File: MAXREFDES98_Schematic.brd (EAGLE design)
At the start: 87.8 x 25.4 mm, 34 parts, among them U1 MB110S-TP, U2 MB110S-TP, U3 MAX5969AETB+

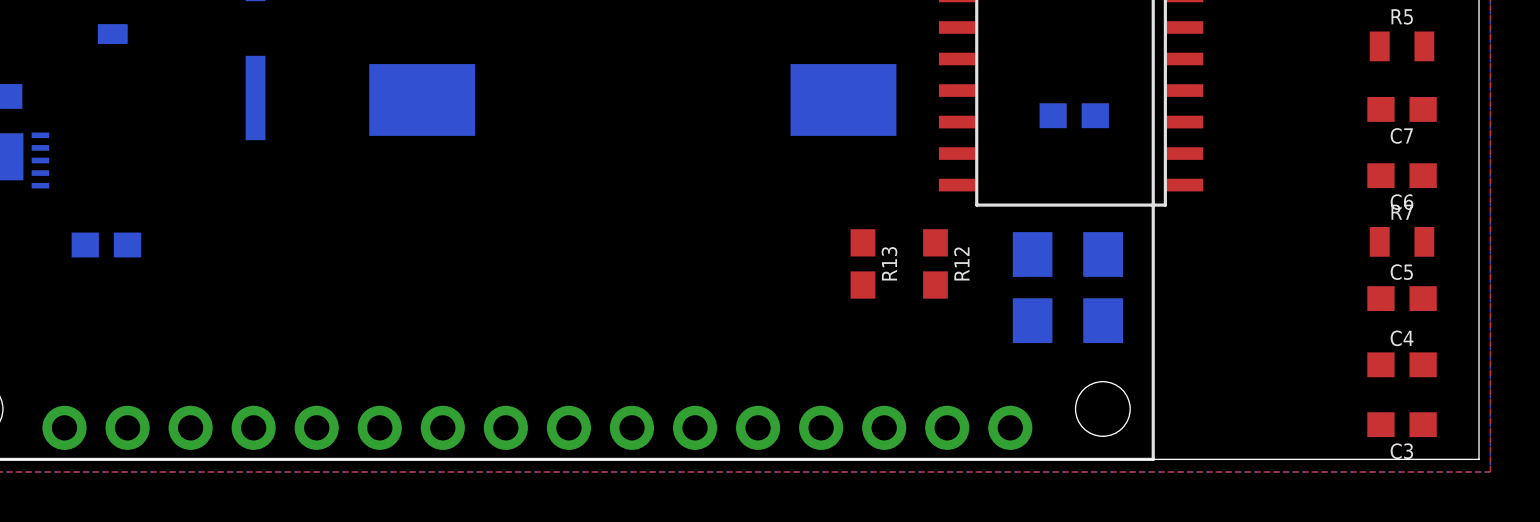
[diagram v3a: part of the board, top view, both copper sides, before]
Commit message: Added new caps and leds
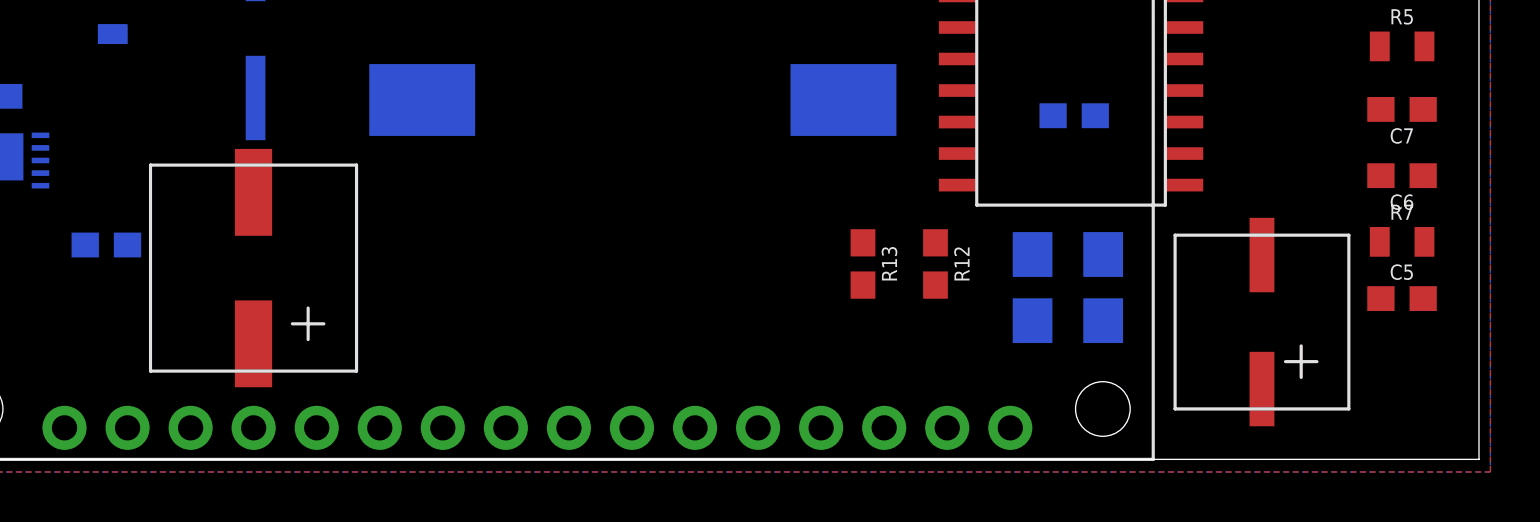
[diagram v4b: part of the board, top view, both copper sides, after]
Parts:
- C3: value 330uF -> 337AXZ025M; device SparkFun-Capacitors:0603 -> CameraBoard_Library:337AXZ025M
- C4: value 220uF -> EXV227M016A9HAA; device SparkFun-Capacitors:0603 -> CameraBoard_Library:EXV227M016A9HAA
- D3: value (none) -> GREEN
- D4: value (none) -> AMBER
- moved C3 47.0 mm to (38.1, 7.37), turned to 0 degrees
- moved C4 9.32 mm to (75.6, 2.03)
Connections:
- net 5V_OUT: now also C3.PLUS; no longer C3.1
- net GND: now also C3.MINUS, C4.MINUS; no longer C3.2, C4.2
- net VDD: now also C4.PLUS; no longer C4.1
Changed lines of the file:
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@@
 </element>
 <element name="U$1" library="Camera_Board_Parts_09_30_2020" package="L4978D013TR" package3d_urn="urn:adsk.eagle:package:24353853/1" value="L4978D013TR" x="71.374" y="15.494" smashed="yes"/>
-<element name="C3" library="SparkFun-Capacitors" library_urn="urn:adsk.eagle:library:510" package="0603" package3d_urn="urn:adsk.eagle:package:37414/1" value="330uF" x="84.709" y="1.397" smashed="yes" rot="R180">
-<attribute name="NAME" x="84.709" y="0.635" size="0.6096" layer="25" font="vector" ratio="20" rot="R180" align="bottom-center"/>
-<attribute name="PROD_ID" value="CAP-08280" x="84.709" y="1.397" size="1.778" layer="27" rot="R180" display="off"/>
-<attribute name="VALUE" x="84.709" y="2.159" size="0.6096" layer="27" font="vector" ratio="20" rot="R180" align="top-center"/>
-</element>
-<element name="C4" library="SparkFun-Capacitors" library_urn="urn:adsk.eagle:library:510" package="0603" package3d_urn="urn:adsk.eagle:package:37414/1" value="220uF" x="84.709" y="3.81" smashed="yes">
-<attribute name="NAME" x="84.709" y="4.572" size="0.6096" layer="25" font="vector" ratio="20" align="bottom-center"/>
-<attribute name="PROD_ID" value="CAP-08280" x="84.836" y="3.81" size="1.778" layer="27" display="off"/>
-<attribute name="VALUE" x="84.709" y="3.048" size="0.6096" layer="27" font="vector" ratio="20" align="top-center"/>
-</element>
 <element name="C5" library="SparkFun-Capacitors" library_urn="urn:adsk.eagle:library:510" package="0603" package3d_urn="urn:adsk.eagle:package:37414/1" value="220nF" x="84.709" y="6.477" smashed="yes">
 <attribute name="NAME" x="84.709" y="7.239" size="0.6096" layer="25" font="vector" ratio="20" align="bottom-center"/>
@@
 <attribute name="VENDOR" value="STMicroelectronics" x="78.867" y="22.606" size="1.778" layer="28" rot="MR180" display="off"/>
 </element>
-<element name="D3" library="SparkFun-LED" library_urn="urn:adsk.eagle:library:529" package="FKIT-LED-1206" package3d_urn="urn:adsk.eagle:package:39355/1" value="" x="71.247" y="8.255" smashed="yes" rot="MR0">
+<element name="D3" library="SparkFun-LED" library_urn="urn:adsk.eagle:library:529" package="FKIT-LED-1206" package3d_urn="urn:adsk.eagle:package:39355/1" value="GREEN" x="71.247" y="8.255" smashed="yes" rot="MR0">
 <attribute name="NAME" x="71.247" y="9.36625" size="0.6096" layer="26" font="vector" ratio="20" rot="MR0" align="bottom-center"/>
 <attribute name="VALUE" x="71.247" y="7.14375" size="0.6096" layer="28" font="vector" ratio="20" rot="MR0" align="top-center"/>
 </element>
-<element name="D4" library="SparkFun-LED" library_urn="urn:adsk.eagle:library:529" package="FKIT-LED-1206" package3d_urn="urn:adsk.eagle:package:39355/1" value="" x="71.247" y="5.588" smashed="yes" rot="MR0">
+<element name="D4" library="SparkFun-LED" library_urn="urn:adsk.eagle:library:529" package="FKIT-LED-1206" package3d_urn="urn:adsk.eagle:package:39355/1" value="AMBER" x="71.247" y="5.588" smashed="yes" rot="MR0">
 <attribute name="NAME" x="71.247" y="6.69925" size="0.6096" layer="26" font="vector" ratio="20" rot="MR0" align="bottom-center"/>
 <attribute name="VALUE" x="71.247" y="4.47675" size="0.6096" layer="28" font="vector" ratio="20" rot="MR0" align="top-center"/>
@@
 </element>
 <element name="U$2" library="CameraBoard_Library" package="NANO_PI_CLEAN" value="NANO_PI_CLEAN" x="19.685" y="0" smashed="yes"/>
+<element name="C4" library="CameraBoard_Library" package="EXV227M016A9HAA" value="EXV227M016A9HAA" x="75.565" y="2.032" smashed="yes"/>
+<element name="C3" library="CameraBoard_Library" package="337AXZ025M" value="337AXZ025M" x="38.1" y="7.366" smashed="yes"/>
 </elements>
 <signals>
@@
 <contactref element="L1" pad="P$1"/>
 <contactref element="U$1" pad="11"/>
-<contactref element="C4" pad="1"/>
 <contactref element="C5" pad="1"/>
 <contactref element="R7" pad="1"/>
@@
 <contactref element="C2" pad="PLUS"/>
 <contactref element="L1" pad="P$2"/>
-<wire x1="83.859" y1="6.477" x2="83.809" y2="8.763" width="0" layer="19" extent="1-1"/>
-<wire x1="83.859" y1="3.81" x2="83.859" y2="6.477" width="0" layer="19" extent="1-1"/>
-<wire x1="75.9365" y1="13.589" x2="83.859" y2="6.477" width="0" layer="19" extent="1-1"/>
+<contactref element="C4" pad="PLUS"/>
+<wire x1="83.809" y1="8.763" x2="83.859" y2="6.477" width="0" layer="19" extent="1-1"/>
+<wire x1="75.9365" y1="13.589" x2="83.809" y2="8.763" width="0" layer="19" extent="1-1"/>
 <wire x1="38.522" y1="14.558" x2="75.9365" y2="13.589" width="0" layer="19" extent="1-16"/>
 <wire x1="32.766" y1="18.934" x2="38.522" y2="14.558" width="0" layer="19" extent="16-16"/>
@@
 <wire x1="26.582" y1="11.0235" x2="28.128" y2="14.623" width="0" layer="19" extent="16-16"/>
 <wire x1="26.631" y1="8.636" x2="26.582" y2="11.0235" width="0" layer="19" extent="16-16"/>
+<wire x1="22.531" y1="19.197" x2="28.128" y2="20.043" width="0" layer="19" extent="16-16"/>
+<wire x1="17.984" y1="21.317" x2="22.531" y2="19.197" width="0" layer="19" extent="16-16"/>
 <wire x1="33.362" y1="8.636" x2="26.631" y2="8.636" width="0" layer="19" extent="16-16"/>
-<wire x1="22.531" y1="19.197" x2="28.128" y2="14.623" width="0" layer="19" extent="16-16"/>
 <wire x1="17.984" y1="12.846" x2="22.531" y2="19.197" width="0" layer="19" extent="1-16"/>
-<wire x1="17.984" y1="21.317" x2="22.531" y2="19.197" width="0" layer="19" extent="16-16"/>
+<wire x1="79.065" y1="2.832" x2="17.984" y2="12.846" width="0" layer="19" extent="1-1"/>
 </signal>
 <signal name="VSS_EP">
@@
 <contactref element="R8" pad="1"/>
 <contactref element="R11" pad="1"/>
-<contactref element="C3" pad="1"/>
 <contactref element="R4" pad="2"/>
 <contactref element="L2_150UH" pad="1"/>
 <contactref element="U$2" pad="5V"/>
 <contactref element="U$2" pad="5V_2"/>
-<wire x1="85.559" y1="1.397" x2="85.609" y2="19.304" width="0" layer="19" extent="1-1"/>
+<contactref element="C3" pad="PLUS"/>
 <wire x1="45.2374" y1="14.478" x2="85.609" y2="19.304" width="0" layer="19" extent="1-16"/>
-<wire x1="3.722" y1="13.843" x2="45.2374" y2="14.478" width="0" layer="19" extent="16-16"/>
+<wire x1="33.3658" y1="1.27" x2="45.2374" y2="14.478" width="0" layer="19" extent="16-16"/>
+<wire x1="30.8258" y1="1.27" x2="33.3658" y2="1.27" width="0" layer="19" extent="1-1"/>
+<wire x1="3.722" y1="13.843" x2="30.8258" y2="1.27" width="0" layer="19" extent="16-16"/>
 <wire x1="3.722" y1="21.336" x2="3.722" y2="13.843" width="0" layer="19" extent="16-16"/>
-<wire x1="30.8258" y1="1.27" x2="3.722" y2="13.843" width="0" layer="19" extent="16-16"/>
-<wire x1="33.3658" y1="1.27" x2="30.8258" y2="1.27" width="0" layer="19" extent="1-1"/>
+<wire x1="38.44" y1="4.656" x2="3.722" y2="13.843" width="0" layer="19" extent="1-16"/>
 </signal>
 <signal name="FB">
@@
 <contactref element="C8" pad="2"/>
 <contactref element="R6" pad="1"/>
-<contactref element="C4" pad="2"/>
 <contactref element="D2" pad="2"/>
-<contactref element="C3" pad="2"/>
 <contactref element="D3" pad="C"/>
 <contactref element="D4" pad="C"/>
 <contactref element="U$2" pad="GND"/>
+<contactref element="C4" pad="MINUS"/>
+<contactref element="C3" pad="MINUS"/>
 <wire x1="85.609" y1="21.717" x2="85.559" y2="24.13" width="0" layer="19" extent="1-1"/>
+<wire x1="80.9117" y1="22.606" x2="85.609" y2="21.717" width="0" layer="19" extent="1-16"/>
 <wire x1="83.859" y1="14.097" x2="85.609" y2="21.717" width="0" layer="19" extent="1-1"/>
 <wire x1="83.859" y1="11.43" x2="83.859" y2="14.097" width="0" layer="19" extent="1-1"/>
 <wire x1="85.559" y1="6.477" x2="83.859" y2="11.43" width="0" layer="19" extent="1-1"/>
-<wire x1="85.559" y1="3.81" x2="85.559" y2="6.477" width="0" layer="19" extent="1-1"/>
-<wire x1="83.859" y1="1.397" x2="85.559" y2="3.81" width="0" layer="19" extent="1-1"/>
-<wire x1="69.825" y1="8.255" x2="83.859" y2="11.43" width="0" layer="19" extent="1-1"/>
-<wire x1="69.825" y1="5.588" x2="69.825" y2="8.255" width="0" layer="19" extent="1-1"/>
-<wire x1="80.9117" y1="22.606" x2="85.609" y2="21.717" width="0" layer="19" extent="1-16"/>
-<wire x1="38.522" y1="20.158" x2="80.9117" y2="22.606" width="0" layer="19" extent="16-16"/>
+<wire x1="69.825" y1="8.255" x2="83.859" y2="11.43" width="0" layer="19" extent="1-16"/>
+<wire x1="69.825" y1="5.588" x2="69.825" y2="8.255" width="0" layer="19" extent="16-16"/>
+<wire x1="38.522" y1="20.158" x2="69.825" y2="8.255" width="0" layer="19" extent="16-16"/>
+<wire x1="35.9058" y1="24.13" x2="38.522" y2="20.158" width="0" layer="19" extent="16-16"/>
 <wire x1="29.857" y1="13.0555" x2="38.522" y2="20.158" width="0" layer="19" extent="16-16"/>
 <wire x1="29.857" y1="12.5475" x2="29.857" y2="13.0555" width="0" layer="19" extent="16-16"/>
-<wire x1="35.9058" y1="24.13" x2="29.857" y2="12.5475" width="0" layer="19" extent="16-16"/>
-<wire x1="3.722" y1="16.256" x2="35.9058" y2="24.13" width="0" layer="19" extent="16-16"/>
+<wire x1="3.722" y1="16.256" x2="29.857" y2="13.0555" width="0" layer="19" extent="16-16"/>
 <wire x1="3.722" y1="18.669" x2="3.722" y2="16.256" width="0" layer="19" extent="16-16"/>
+<wire x1="79.065" y1="8.232" x2="3.722" y2="16.256" width="0" layer="19" extent="1-16"/>
+<wire x1="38.44" y1="10.756" x2="79.065" y2="8.232" width="0" layer="19" extent="1-1"/>
 </signal>
 <signal name="CLS">

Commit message: Placement
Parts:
- moved C3 57.0 mm to (94.6, 14.9), turned to 90 degrees
- moved L2_150UH 46.7 mm to (98.8, 2.29), flipped to the top, turned to 0 degrees
- moved C4 35.2 mm to (44.6, 18.7), turned to 270 degrees
- moved C5 30.7 mm to (55.9, 17.1)
- moved U$2 25.5 mm to (17.8, 25.4), flipped to the bottom, turned to 180 degrees
- moved R5 25.3 mm to (59.4, 17.1)
- moved U$1 14.6 mm to (57.8, 10.0)
- moved C2 11.5 mm to (35.8, 3.94), flipped to the top
- moved R13 10.5 mm to (68.2, 17.0)
- moved R10 10.0 mm to (4.83, 8.64)
- moved R9 10.0 mm to (4.83, 6.22)
- moved R11 10.0 mm to (4.83, 3.81)
- moved R8 10.0 mm to (4.83, 11.3)
- moved R12 9.48 mm to (64.6, 17.3)
- moved U1 9.14 mm to (10.2, 12.7)
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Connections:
- new net VDD_L: C2.PLUS, C4.PLUS, C5.1, L1.P$2, R3.2, R7.1, U$1.11
- net RD+: now also CONN.1; no longer CONN.5
- net RD-: now also CONN.2; no longer CONN.6
- net RECT1_IN_MINUS: now also CONN.6; no longer CONN.2
- net RECT1_IN_PLUS: now also CONN.5; no longer CONN.1
- net RECT2_IN_MINUS: now also CONN.7; no longer CONN.3
- net RECT2_IN_PLUS: now also CONN.8; no longer CONN.4
- net TD+: now also CONN.3; no longer CONN.7
- net TD-: now also CONN.4; no longer CONN.8
- net VDD: no longer C2.PLUS, C4.PLUS, C5.1, L1.P$2, R3.2, R7.1, U$1.11
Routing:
- net TD+: track 0.00 -> 59.6 mm
- net TD-: track 0.00 -> 59.4 mm
- net 5V_OUT: track 0.00 -> 52.9 mm
- net RD+: track 0.00 -> 52.8 mm
- net RD-: track 0.00 -> 50.0 mm
- net VDD: track 0.00 -> 47.3 mm, vias 0 -> 4
- net VSS_EP: track 0.00 -> 33.6 mm, vias 0 -> 2
- net VDD_L: track 0.00 -> 33.3 mm, vias 0 -> 2
- net PG_EN/SS_INH: track 0.00 -> 29.2 mm
- net CLS: track 0.00 -> 14.9 mm
- net RECT1_IN_PLUS: track 0.00 -> 6.13 mm
- net RECT1_IN_MINUS: track 0.00 -> 6.06 mm
- net RECT2_IN_MINUS: track 0.00 -> 5.30 mm
- net RECT2_IN_PLUS: track 0.00 -> 5.25 mm
- net DET: track 0.00 -> 3.44 mm
- added copper zone on layer 16, net DET
- added copper zone on layer 16, net PG_EN/SS_INH

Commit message: Update MAXREFDES98_Schematic.brd
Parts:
- moved C8 39.2 mm to (49.1, 7.75), turned to 180 degrees
- moved R6 30.7 mm to (57.8, 6.99), flipped to the bottom
- moved R4 27.8 mm to (57.8, 12.2), flipped to the bottom
- moved C7 22.1 mm to (63.0, 18.0), turned to 90 degrees
- moved R7 17.5 mm to (67.6, 5.46), turned to 90 degrees
- moved C6 17.3 mm to (67.7, 8.13), turned to 0 degrees
- moved C3 15.0 mm to (79.6, 15.7)
- moved L2_150UH 13.8 mm to (85.0, 2.29), turned to 180 degrees
- moved D4 11.4 mm to (68.2, 16.9), turned to 270 degrees
- moved D3 9.90 mm to (65.7, 16.9), turned to 270 degrees
- moved C9 4.90 mm to (67.6, 10.9), flipped to the top, turned to 90 degrees
- moved R13 4.06 mm to (68.2, 21.1), turned to 90 degrees
- moved R12 3.82 mm to (65.7, 21.0), turned to 90 degrees
- moved D2 1.14 mm to (77.7, 22.6)
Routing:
- net PG_EN/SS_INH: track 29.2 -> 36.6 mm, vias 0 -> 1

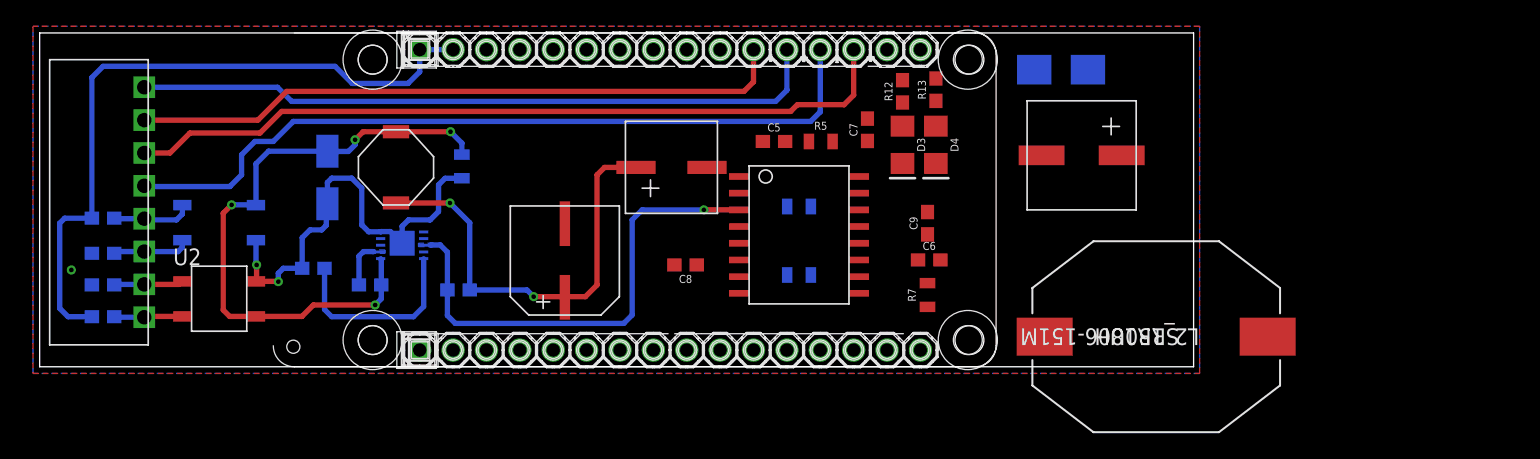
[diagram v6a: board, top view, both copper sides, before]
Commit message: Board all wired up
Board is all wried up, DRC is passed
Board is also smaller now as well
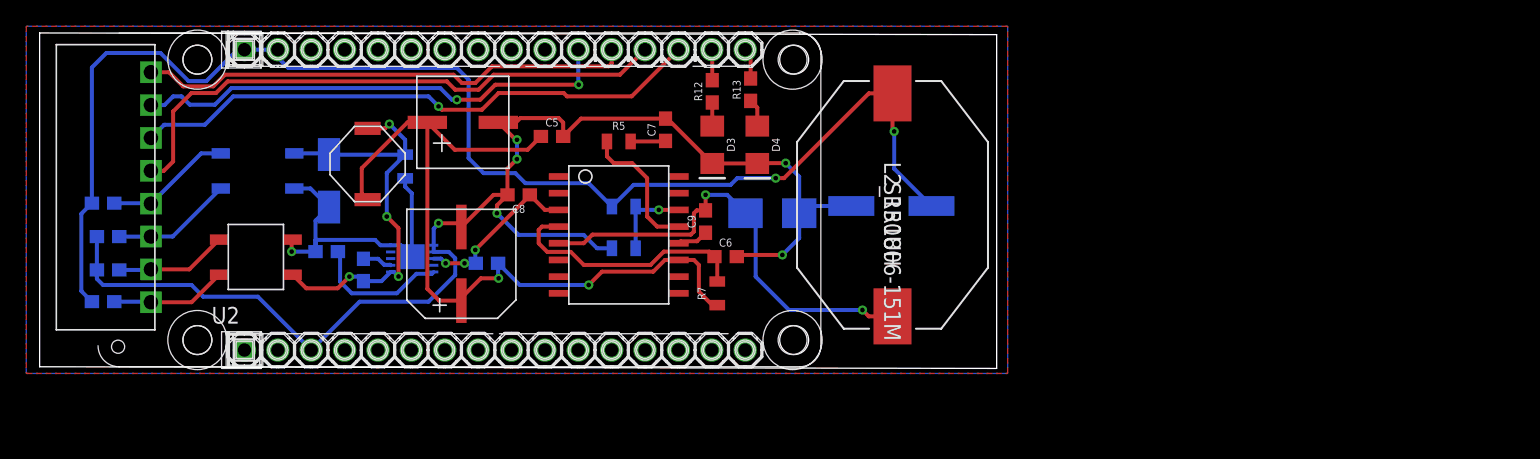
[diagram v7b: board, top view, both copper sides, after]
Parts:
- moved D2 24.5 mm to (55.8, 11.7)
- moved L2_150UH 22.4 mm to (64.9, 12.3), turned to 270 degrees
- moved C5 16.9 mm to (39.0, 17.5)
- moved C9 16.9 mm to (50.7, 11.0)
- moved C4 16.2 mm to (28.7, 22.1)
- moved R7 16.0 mm to (51.6, 5.59)
- moved C6 15.5 mm to (52.2, 8.38)
- moved C7 15.4 mm to (47.6, 18.0)
- moved R5 15.4 mm to (44.1, 17.1)
- moved C3 14.8 mm to (65.2, 12.6), flipped to the bottom, turned to 270 degrees
- moved D3 14.5 mm to (51.2, 16.9)
- moved R12 14.5 mm to (51.2, 21.0)
- moved R13 14.1 mm to (54.1, 21.1)
- moved C8 13.8 mm to (36.4, 13.1)
- moved U$1 13.7 mm to (44.1, 10.0)
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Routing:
- net GND: track 0.00 -> 106.0 mm, vias 1 -> 6
- net 5V_OUT: track 52.9 -> 103.9 mm, vias 0 -> 2
- net IND_IN: track 0.00 -> 34.6 mm, vias 0 -> 2
- net VDD_L: track 33.3 -> 60.2 mm
- net PG_EN/SS_INH: track 36.6 -> 13.1 mm, vias 1 -> 3
- net OSC: track 0.00 -> 19.3 mm
- net TD+: track 59.3 -> 44.0 mm, vias 0 -> 1
- net TD-: track 59.4 -> 44.2 mm
- net RD+: track 52.8 -> 37.8 mm
- net VDD: track 47.3 -> 32.7 mm
- net RD-: track 50.0 -> 37.1 mm, vias 0 -> 2
- net COMP: track 0.00 -> 10.5 mm
- net VSS_EP: track 33.6 -> 24.8 mm, vias 2 -> 1
- net FB: track 0.00 -> 6.46 mm, vias 0 -> 1
- net CLS: track 14.9 -> 10.5 mm
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- removed copper zone on layer 16, net DET
- removed copper zone on layer 16, net PG_EN/SS_INH
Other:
- board size 87.8 x 25.4 mm -> 72.8 x 25.5 mm
